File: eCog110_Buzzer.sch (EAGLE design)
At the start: 1 part

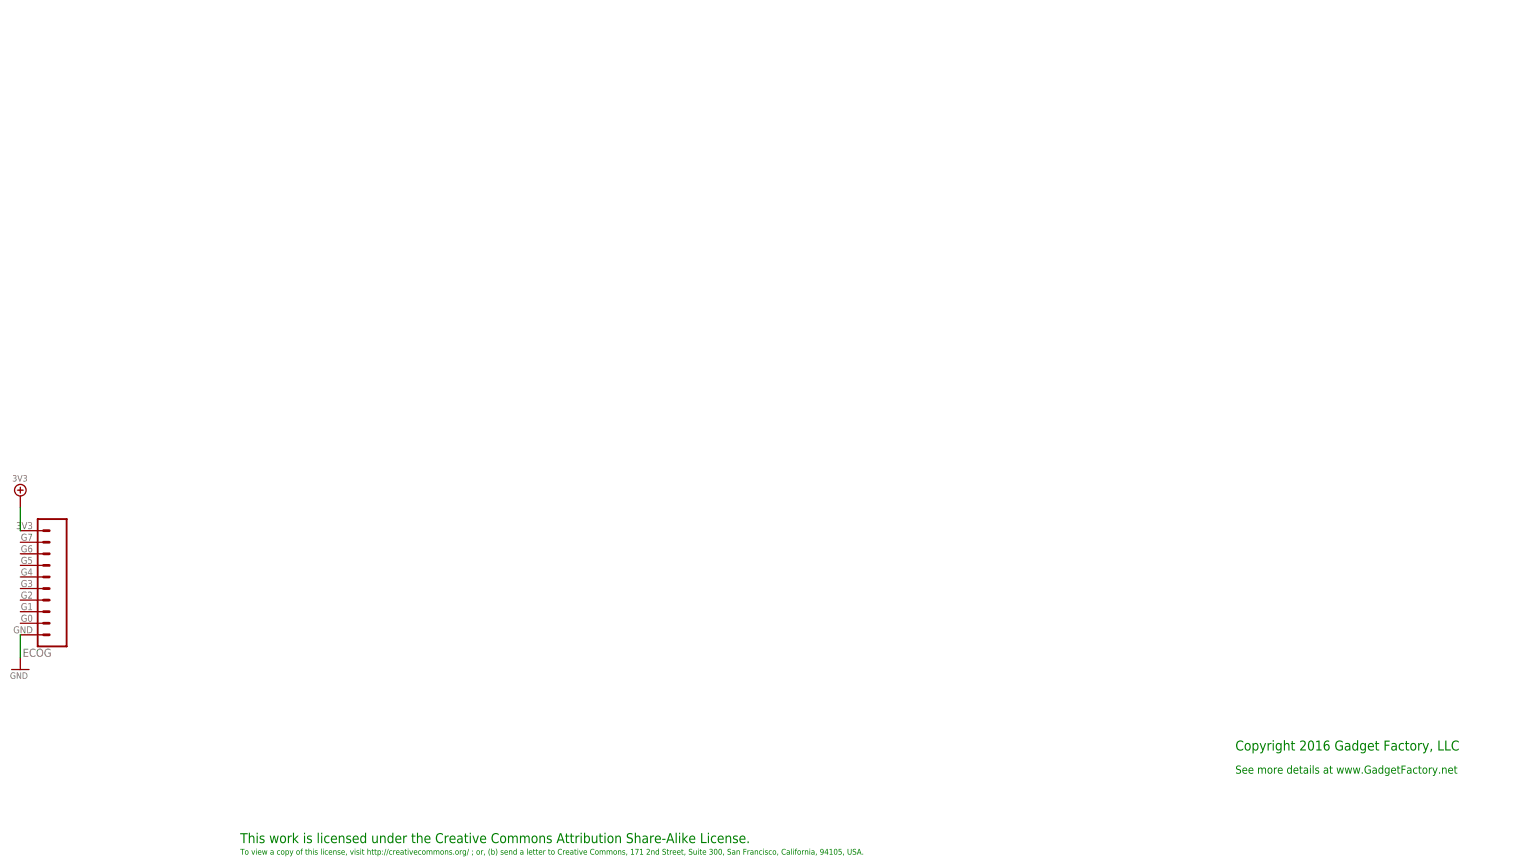
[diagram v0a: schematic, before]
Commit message: Added new eCogs
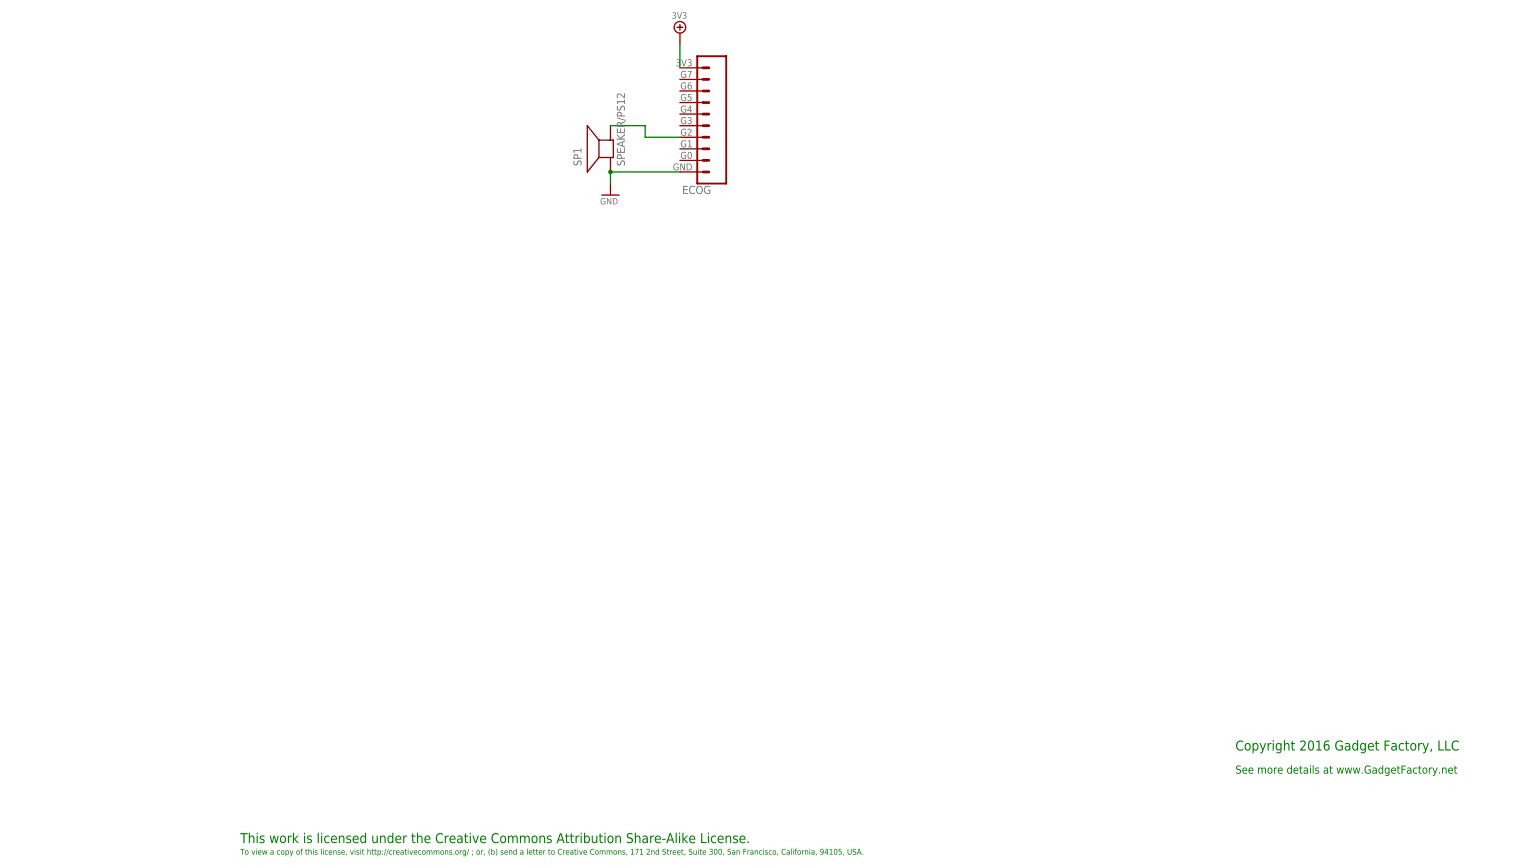
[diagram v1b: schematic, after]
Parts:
- added SP1: SPEAKER/PS12, adafruit:SPEAKER/PS12
- ECOG: PARTNO (none) -> NREC010SABC-M30RC,SULLINS CONNECTOR SOLUTIONS,dk,S1013EC-10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
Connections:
- new net N$1: ECOG.G2, SP1.-
- net GND: now also SP1.+
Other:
- moved on the sheet: ECOG
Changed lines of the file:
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@@
 <parts>
 <part name="FRAME1" library="frames" deviceset="A3L-LOC" device=""/>
-<part name="ECOG" library="eCogs" deviceset="ECOG_GENERAL_ROW" device="ECOG_GENERAL_SMD" value="ECOG_GENERAL_ROWECOG_GENERAL_SMD"/>
+<part name="ECOG" library="eCogs" deviceset="ECOG_GENERAL_ROW" device="ECOG_GENERAL_SMD" value="ECOG_GENERAL_ROWECOG_GENERAL_SMD">
+<attribute name="PARTNO" value="NREC010SABC-M30RC,SULLINS CONNECTOR SOLUTIONS,dk,S1013EC-10-ND,&quot;10 Positions Header, Unshrouded Connector 0.100&quot;&quot; (2.54mm) Surface Mount Tin eCog&quot;, REF78"/>
+</part>
 <part name="3V3_PWR1" library="eCogs" deviceset="3V3" device=""/>
 <part name="GND1" library="eCogs" deviceset="GND" device=""/>
+<part name="SP1" library="adafruit" deviceset="SPEAKER" device="/PS12">
+<attribute name="DIGIKEY" value="445-2525-1-ND"/>
+<attribute name="PARTNO" value="PS1240P02BT,TDK CORPORATION (VA),dk,445-2525-1-ND,&quot;Zero-Peak Signal Buzzer Single Tone 4kHz Piezo 30V (Max) 60dB @ 3V, 10cm &quot;, REF77"/>
+</part>
 </parts>
 <sheets>
@@
 <instances>
 <instance part="FRAME1" gate="G$1" x="0" y="0"/>
-<instance part="ECOG" gate="ECOG_GENERAL" x="55.88" y="53.34"/>
-<instance part="3V3_PWR1" gate="A" x="50.8" y="86.36"/>
-<instance part="GND1" gate="A" x="50.8" y="48.26"/>
+<instance part="ECOG" gate="ECOG_GENERAL" x="200.66" y="154.94">
+<attribute name="PARTNO" x="200.66" y="154.94" size="1.778" layer="96" display="off"/>
+</instance>
+<instance part="3V3_PWR1" gate="A" x="195.58" y="187.96"/>
+<instance part="GND1" gate="A" x="180.34" y="152.4"/>
+<instance part="SP1" gate="S1" x="180.34" y="162.56" rot="R90">
+<attribute name="DIGIKEY" x="180.34" y="162.56" size="1.778" layer="96" rot="R90" display="off"/>
+<attribute name="PARTNO" x="180.34" y="162.56" size="1.778" layer="96" display="off"/>
+</instance>
 </instances>
 <busses>
@@
 <pinref part="ECOG" gate="ECOG_GENERAL" pin="3V3"/>
 <pinref part="3V3_PWR1" gate="A" pin="3V3"/>
-<wire x1="50.8" y1="83.82" x2="50.8" y2="78.74" width="0.1524" layer="91"/>
+<wire x1="195.58" y1="180.34" x2="195.58" y2="185.42" width="0.2032" layer="91"/>
 </segment>
 </net>
@@
 <pinref part="ECOG" gate="ECOG_GENERAL" pin="GND"/>
 <pinref part="GND1" gate="A" pin="GND"/>
-<wire x1="50.8" y1="55.88" x2="50.8" y2="50.8" width="0.2032" layer="91"/>
+<wire x1="195.58" y1="157.48" x2="180.34" y2="157.48" width="0.2032" layer="91"/>
+<wire x1="180.34" y1="157.48" x2="180.34" y2="154.94" width="0.2032" layer="91"/>
+<pinref part="SP1" gate="S1" pin="+"/>
+<junction x="180.34" y="157.48"/>
 </segment>
 </net>
+<net name="N$1" class="0">
+<segment>
+<pinref part="ECOG" gate="ECOG_GENERAL" pin="G2"/>
+<wire x1="195.58" y1="165.1" x2="187.96" y2="165.1" width="0.2032" layer="91"/>
+<wire x1="187.96" y1="165.1" x2="187.96" y2="167.64" width="0.2032" layer="91"/>
+<pinref part="SP1" gate="S1" pin="-"/>
+<wire x1="187.96" y1="167.64" x2="180.34" y2="167.64" width="0.2032" layer="91"/>
+</segment>
+</net>
